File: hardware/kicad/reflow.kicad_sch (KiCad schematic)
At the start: 33 parts, among them J1 24V_IN, J2 HEATER, J3 MAX31855, J4 OLED, Q1 IRFS4710, Q2 BS170, Q3 BS170, SW1 ENC, SW2 START, U2 LM2576-5.0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

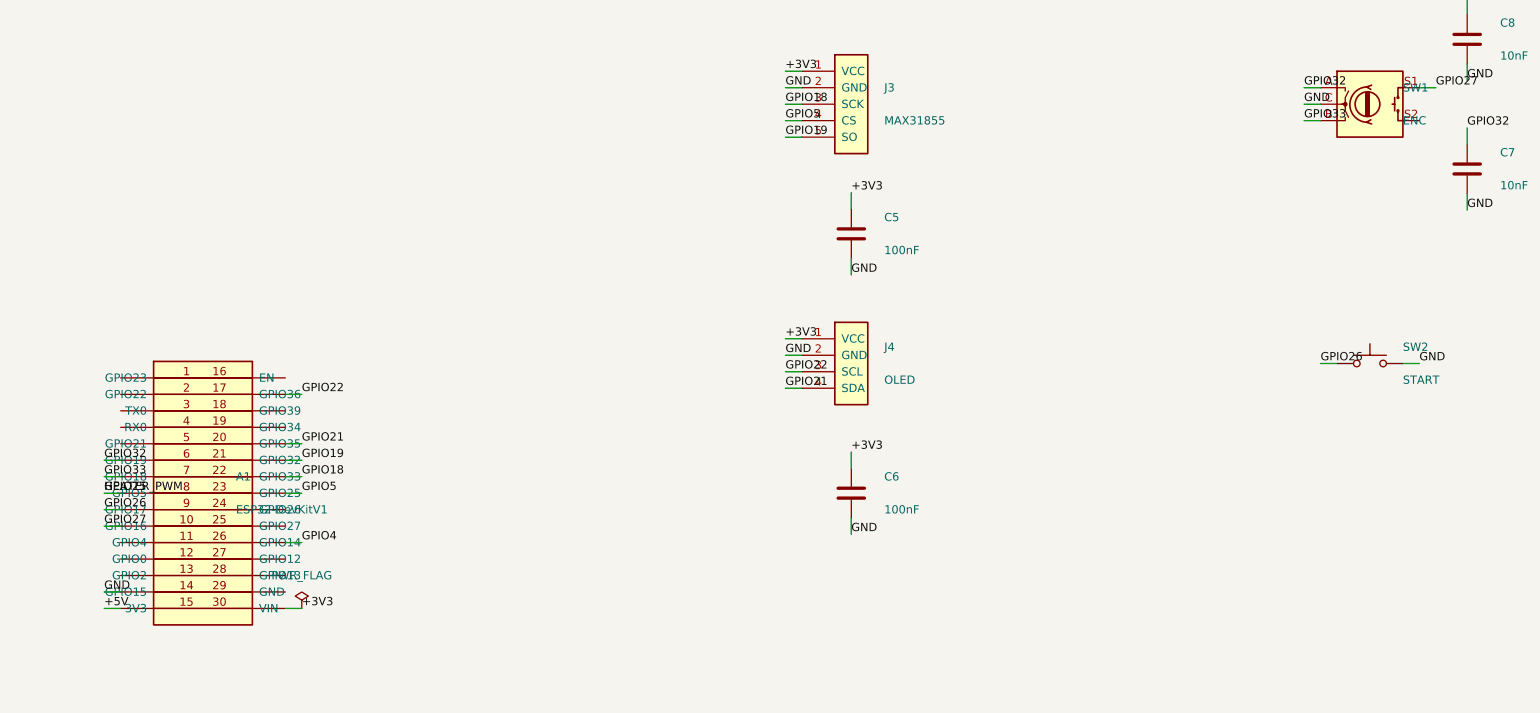
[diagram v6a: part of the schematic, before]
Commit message: hardware: assign footprints, ERC clean, finalize electrical calcs
- Q2/Q3 (BS170): new energy_system:TO-92_Inline_GDS footprint with NUMERIC
  pads 1/2/3 placed at the BS170 physical legs (left=Drain, mid=Gate,
  right=Source per ON Semi BS170/D Rev2). Numeric pads are required because
  the stock Q_NMOS_GDS symbol numbers its pins 1/2/3; pcb_build.py and KiCad
  both bind pad-name to pin-number, so G/D/S-named pads would get no net.
- Q1 (IRFS4710): switch to plain numeric TO-220-3_Vertical_LaserPads (the
  _GDS pad-named variant would also get no net). Pinout 1=G/2=D/3=S verified
  against the IR IRFB/IRFS/IRFL4710 datasheet.
- U2 (LM2576T-5): hand-authored TO-220-5_Vertical_LaserPads at 2.54mm pitch
  (the stock 1.7mm-pitch Pentawatt fails the 0.8mm laser clearance). Pads 1-5
  = Vin/Out/GND/FB/ON-OFF.
- Add 17 no_connect directives on intentionally-unused ESP32 spare pins and
  SW1.S2 -> full ERC exits 0 (was 18 errors).
- Fix three stale stock footprint names (fuse holder, toroid, encoder) and
  register the stock footprint libs in the project fp-lib-table so
  verify_footprints resolves 38/38.
- Add tools/verify_pad_nets.py: simulates pcb_build.py pad->net binding for
  Q1/Q2/Q3/U2 and asserts every pad gets a net (safety gate for the board).
- docs/electrical-calcs.md: add IPC-2221 pour-width requirement for the 13 A
  heater nets (>=8 mm target, 6.8 mm IPC floor at dT=20C on 1 oz copper).
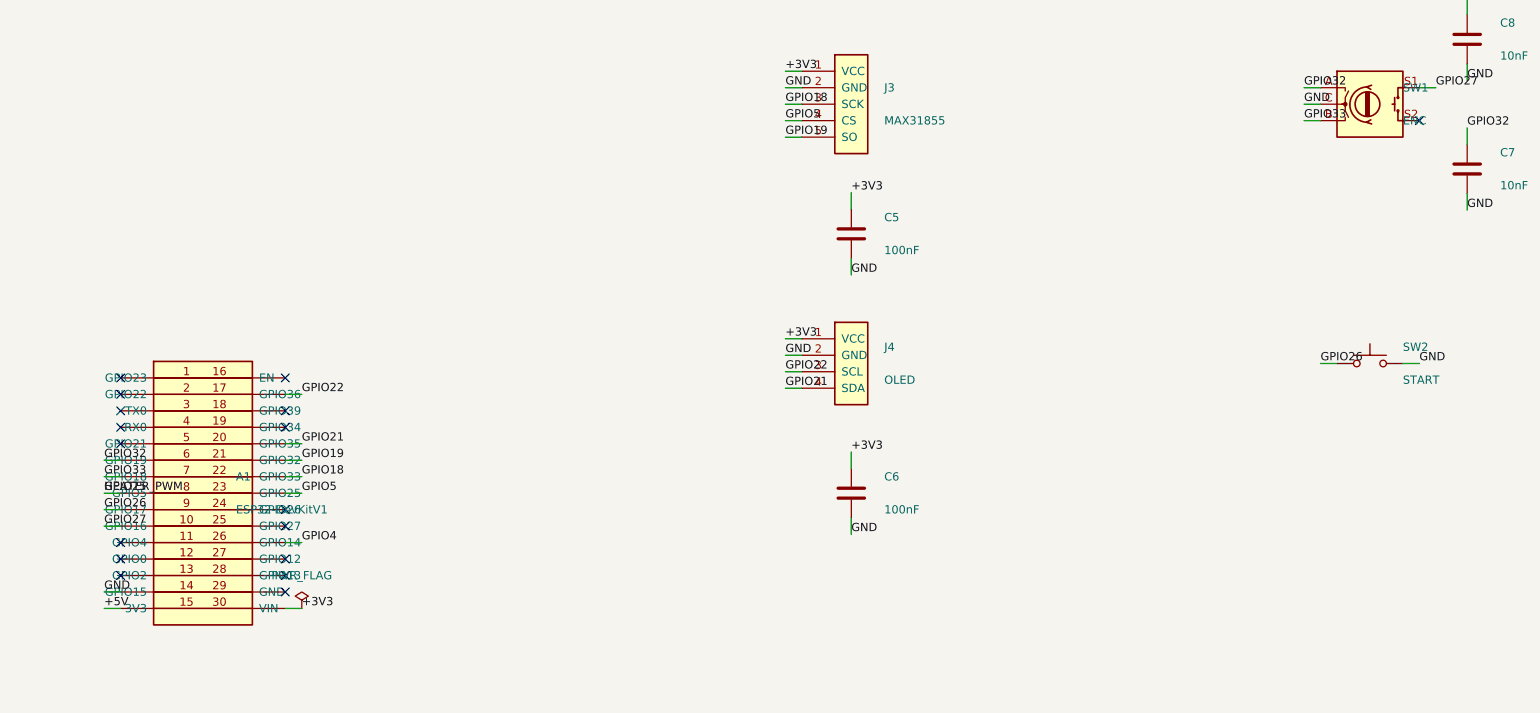
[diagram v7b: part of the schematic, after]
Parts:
- F1: footprint Fuse:Fuseholder_Cylinder-5x20mm_Schurter_FAB_0031.8201_Horizontal_Closed -> Fuse:Fuseholder_Cylinder-5x20mm_Schurter_FUP_0031.2510_Horizontal_Closed
- L1: footprint Inductor_THT:L_Toroid_Vertical_L20.0mm_D7.0mm_P10.16mm -> Inductor_THT:L_Toroid_Vertical_L26.7mm_W14.0mm_P10.16mm_Pulse_D
- Q1: footprint energy_system:TO-220-3_Vertical_LaserPads_GDS -> energy_system:TO-220-3_Vertical_LaserPads
- Q2, Q3: footprint Package_TO_SOT_THT:TO-92_Inline -> energy_system:TO-92_Inline_GDS
- SW1: footprint Rotary_Encoder:RotaryEncoder_Alps_EC11E-Switch -> Rotary_Encoder:RotaryEncoder_Alps_EC11E-Switch_Vertical_H20mm
- U2: footprint energy_system:TO-220-3_Vertical_LaserPads -> energy_system:TO-220-5_Vertical_LaserPads
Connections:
- no-connect marks 0 -> 17
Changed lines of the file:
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@@
 			)
 		)
-		(property "Footprint" "Fuse:Fuseholder_Cylinder-5x20mm_Schurter_FAB_0031.8201_Horizontal_Closed"
+		(property "Footprint" "Fuse:Fuseholder_Cylinder-5x20mm_Schurter_FUP_0031.2510_Horizontal_Closed"
 			(at 55 40 0)
 			(effects
@@
 			)
 		)
-		(property "Footprint" "energy_system:TO-220-3_Vertical_LaserPads"
+		(property "Footprint" "energy_system:TO-220-5_Vertical_LaserPads"
 			(at 40 80 0)
 			(effects
@@
 			)
 		)
-		(property "Footprint" "Inductor_THT:L_Toroid_Vertical_L20.0mm_D7.0mm_P10.16mm"
+		(property "Footprint" "Inductor_THT:L_Toroid_Vertical_L26.7mm_W14.0mm_P10.16mm_Pulse_D"
 			(at 70 75 0)
 			(effects
@@
 			)
 		)
-		(property "Footprint" "energy_system:TO-220-3_Vertical_LaserPads_GDS"
+		(property "Footprint" "energy_system:TO-220-3_Vertical_LaserPads"
 			(at 330 220 0)
 			(effects
@@
 			)
 		)
-		(property "Footprint" "Package_TO_SOT_THT:TO-92_Inline"
+		(property "Footprint" "energy_system:TO-92_Inline_GDS"
 			(at 270 230 0)
 			(effects
@@
 			)
 		)
-		(property "Footprint" "Package_TO_SOT_THT:TO-92_Inline"
+		(property "Footprint" "energy_system:TO-92_Inline_GDS"
 			(at 300 230 0)
 			(effects
@@
 			)
 		)
-		(property "Footprint" "Rotary_Encoder:RotaryEncoder_Alps_EC11E-Switch"
+		(property "Footprint" "Rotary_Encoder:RotaryEncoder_Alps_EC11E-Switch_Vertical_H20mm"
 			(at 330 90 0)
 			(effects
@@
 		)
 	)
+	(no_connect
+		(at 137.30 132.22)
+	)
+	(no_connect
+		(at 137.30 134.76)
+	)
+	(no_connect
+		(at 137.30 137.30)
+	)
+	(no_connect
+		(at 137.30 139.84)
+	)
+	(no_connect
+		(at 137.30 142.38)
+	)
+	(no_connect
+		(at 137.30 157.62)
+	)
+	(no_connect
+		(at 137.30 160.16)
+	)
+	(no_connect
+		(at 137.30 162.70)
+	)
+	(no_connect
+		(at 162.70 132.22)
+	)
+	(no_connect
+		(at 162.70 137.30)
+	)
+	(no_connect
+		(at 162.70 139.84)
+	)
+	(no_connect
+		(at 162.70 152.54)
+	)
+	(no_connect
+		(at 162.70 155.08)
+	)
+	(no_connect
+		(at 162.70 160.16)
+	)
+	(no_connect
+		(at 162.70 162.70)
+	)
+	(no_connect
+		(at 162.70 165.24)
+	)
+	(no_connect
+		(at 337.62 92.54)
+	)
 	(sheet_instances

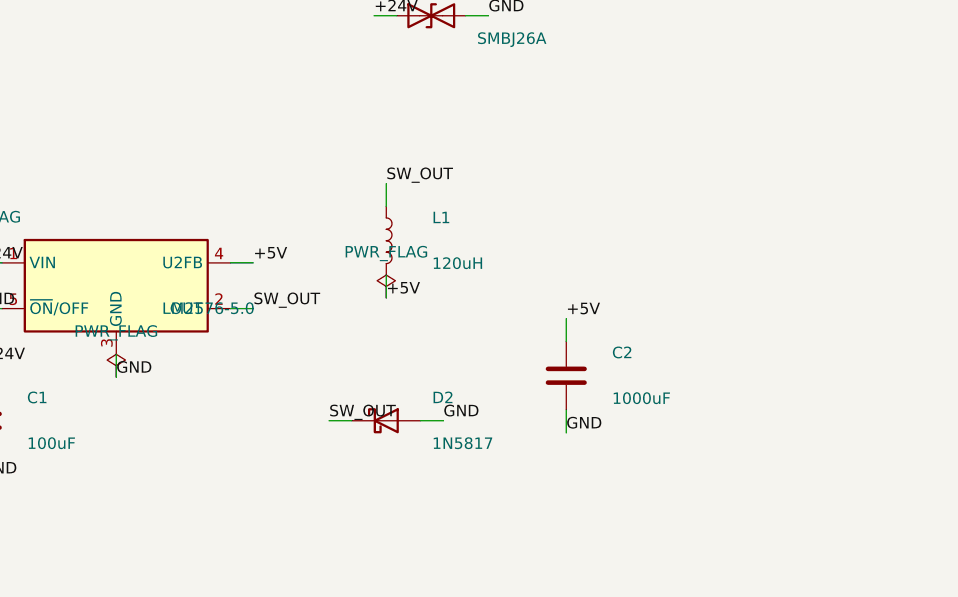
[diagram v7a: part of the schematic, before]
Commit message: hw(buck): swap U2 to LM2575-ADJ with 5.03V feedback divider (R7 3K09 / R8 1K00)
The DTU component shop stocks the adjustable LM2575, not the fixed LM2576-5.0.
Swap U2 to LM2575BT-ADJ (same 5-pin TO-220 pinout/footprint) and add an R7/R8
feedback divider into FB: Vout = 1.23*(1+3090/1000) = 5.03 V. Also fold the
post-placement footprint finalization (5-pin laser pads, GDS variants, real
toroid, fuse holder) and the unused-pin no_connect markers into build_schematic
so it regenerates the finalized schematic faithfully. ERC=0, pad-nets and
boot-safety still pass.
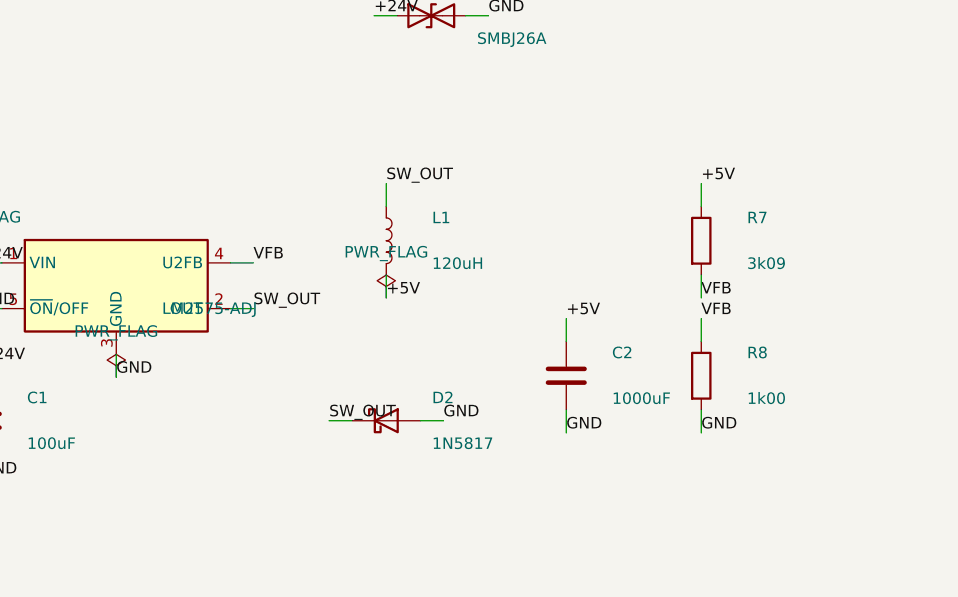
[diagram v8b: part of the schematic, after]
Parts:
- removed U2: LM2576-5.0, energy_system:TO-220-5_Vertical_LaserPads, symbol Regulator_Switching:LM2576T-5
- added R7: 3k09, Resistor_THT:R_Axial_DIN0207_L6.3mm_D2.5mm_P7.62mm_Horizontal, symbol Device:R
- added R8: 1k00, Resistor_THT:R_Axial_DIN0207_L6.3mm_D2.5mm_P7.62mm_Horizontal, symbol Device:R
- added U2: LM2575-ADJ, energy_system:TO-220-5_Vertical_LaserPads, symbol Regulator_Switching:LM2575BT-ADJ
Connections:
- net +24V: now also U2.1 (VIN)
- net +5V: now also R7.1
- net GND: now also R8.2, U2.3 (GND), U2.5 (~{ON}/OFF)
- net SW_OUT: now also U2.2 (OUT)
- new net VFB: R7.2, R8.1, U2.4 (FB)
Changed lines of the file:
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@@
 	)
 	(symbol
-		(lib_id "Regulator_Switching:LM2576T-5")
+		(lib_id "Regulator_Switching:LM2575BT-ADJ")
 		(at 40 80 0)
 		(unit 1)
@@
 			)
 		)
-		(property "Value" "LM2576-5.0"
+		(property "Value" "LM2575-ADJ"
 			(at 45.08 82.54 0)
 			(effects
@@
 	)
 	(symbol
+		(lib_id "Device:R")
+		(at 105 75 0)
+		(unit 1)
+		(exclude_from_sim no)
+		(in_bom yes)
+		(on_board yes)
+		(dnp no)
+		(fields_autoplaced yes)
+		(property "Reference" "R7"
+			(at 110.08 72.46 0)
+			(effects
+				(font
+					(size 1.27 1.27)
+				)
+				(justify left)
+			)
+		)
+		(property "Value" "3k09"
+			(at 110.08 77.54 0)
+			(effects
+				(font
+					(size 1.27 1.27)
+				)
+				(justify left)
+			)
+		)
+		(property "Footprint" "Resistor_THT:R_Axial_DIN0207_L6.3mm_D2.5mm_P7.62mm_Horizontal"
+			(at 105 75 0)
+			(effects
+				(font
+					(size 1.27 1.27)
+				)
+				(hide yes)
+			)
+		)
+		(property "Datasheet" "~"
+			(at 105 75 0)
+			(effects
+				(font
+					(size 1.27 1.27)
+				)
+				(hide yes)
+			)
+		)
+		(property "Description" ""
+			(at 105 75 0)
+			(effects
+				(font
+					(size 1.27 1.27)
+				)
+				(hide yes)
+			)
+		)
+		(pin "1")
+		(pin "2")
+		(instances
+			(project "reflow"
+				(path "/a1b2c3d4-0001-0001-0001-000000000001"
+					(reference "R7")
+					(unit 1)
+				)
+			)
+		)
+	)
+	(symbol
+		(lib_id "Device:R")
+		(at 105 90 0)
+		(unit 1)
+		(exclude_from_sim no)
+		(in_bom yes)
+		(on_board yes)
+		(dnp no)
+		(fields_autoplaced yes)
+		(property "Reference" "R8"
+			(at 110.08 87.46 0)
+			(effects
+				(font
+					(size 1.27 1.27)
+				)
+				(justify left)
+			)
+		)
+		(property "Value" "1k00"
+			(at 110.08 92.54 0)
+			(effects
+				(font
+					(size 1.27 1.27)
+				)
+				(justify left)
+			)
+		)
+		(property "Footprint" "Resistor_THT:R_Axial_DIN0207_L6.3mm_D2.5mm_P7.62mm_Horizontal"
+			(at 105 90 0)
+			(effects
+				(font
+					(size 1.27 1.27)
+				)
+				(hide yes)
+			)
+		)
+		(property "Datasheet" "~"
+			(at 105 90 0)
+			(effects
+				(font
+					(size 1.27 1.27)
+				)
+				(hide yes)
+			)
+		)
+		(property "Description" ""
+			(at 105 90 0)
+			(effects
+				(font
+					(size 1.27 1.27)
+				)
+				(hide yes)
+			)
+		)
+		(pin "1")
+		(pin "2")
+		(instances
+			(project "reflow"
+				(path "/a1b2c3d4-0001-0001-0001-000000000001"
+					(reference "R8")
+					(unit 1)
+				)
+			)
+		)
+	)
+	(symbol
 		(lib_id "Regulator_Linear:LM7812_TO220")
 		(at 40 120 0)
@@
 	(wire
 		(pts
-			(xy 52.7 77.46) (xy 55.24 77.46)
+			(xy 90.0 86.19) (xy 90.0 83.65)
 		)
 		(stroke
@@
 	)
 	(label "+5V"
-		(at 55.24 77.46 0)
+		(at 90.0 83.65 0)
 		(effects
 			(font
@@
 	(wire
 		(pts
-			(xy 90.0 86.19) (xy 90.0 83.65)
+			(xy 105.0 71.19) (xy 105.0 68.65)
 		)
 		(stroke
@@
 	)
 	(label "+5V"
-		(at 90.0 83.65 0)
+		(at 105.0 68.65 0)
+		(effects
+			(font
+				(size 1.27 1.27)
+			)
+			(justify left bottom)
+		)
+	)
+	(wire
+		(pts
+			(xy 105.0 78.81) (xy 105.0 81.35)
+		)
+		(stroke
+			(width 0)
+			(type default)
+		)
+	)
+	(label "VFB"
+		(at 105.0 81.35 0)
+		(effects
+			(font
+				(size 1.27 1.27)
+			)
+			(justify left bottom)
+		)
+	)
+	(wire
+		(pts
+			(xy 52.7 77.46) (xy 55.24 77.46)
+		)
+		(stroke
+			(width 0)
+			(type default)
+		)
+	)
+	(label "VFB"
+		(at 55.24 77.46 0)
+		(effects
+			(font
+				(size 1.27 1.27)
+			)
+			(justify left bottom)
+		)
+	)
+	(wire
+		(pts
+			(xy 105.0 86.19) (xy 105.0 83.65)
+		)
+		(stroke
+			(width 0)
+			(type default)
+		)
+	)
+	(label "VFB"
+		(at 105.0 83.65 0)
+		(effects
+			(font
+				(size 1.27 1.27)
+			)
+			(justify left bottom)
+		)
+	)
+	(wire
+		(pts
+			(xy 105.0 93.81) (xy 105.0 96.35)
+		)
+		(stroke
+			(width 0)
+			(type default)
+		)
+	)
+	(label "GND"
+		(at 105.0 96.35 0)
 		(effects
 			(font
@@
 	)
 	(no_connect
-		(at 137.30 132.22)
+		(at 137.3 132.22)
 	)
 	(no_connect
-		(at 137.30 134.76)
+		(at 137.3 134.76)
 	)
 	(no_connect
-		(at 137.30 137.30)
+		(at 137.3 137.3)
 	)
 	(no_connect
-		(at 137.30 139.84)
+		(at 137.3 139.84)
 	)
 	(no_connect
-		(at 137.30 142.38)
+		(at 137.3 142.38)
 	)
 	(no_connect
-		(at 137.30 157.62)
+		(at 137.3 157.62)
 	)
 	(no_connect
-		(at 137.30 160.16)
+		(at 137.3 160.16)
 	)
 	(no_connect
-		(at 137.30 162.70)
+		(at 137.3 162.7)
 	)
 	(no_connect
-		(at 162.70 132.22)
+		(at 162.7 132.22)
 	)
 	(no_connect
-		(at 162.70 137.30)
+		(at 162.7 137.3)
 	)
 	(no_connect
-		(at 162.70 139.84)
+		(at 162.7 139.84)
 	)
 	(no_connect
-		(at 162.70 152.54)
+		(at 162.7 152.54)
 	)
 	(no_connect
-		(at 162.70 155.08)
+		(at 162.7 155.08)
 	)
 	(no_connect
-		(at 162.70 160.16)
+		(at 162.7 160.16)
 	)
 	(no_connect
-		(at 162.70 162.70)
+		(at 162.7 162.7)
 	)
 	(no_connect
-		(at 162.70 165.24)
+		(at 162.7 165.24)
 	)
 	(no_connect
